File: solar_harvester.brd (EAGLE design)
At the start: 46 x 25.4 mm, 36 parts, among them U1 BQ25505, U2 TPS61322XA, U3 TPS61322XA, U4 MAX17040, U5 INA226, U6 DMP3085LSD

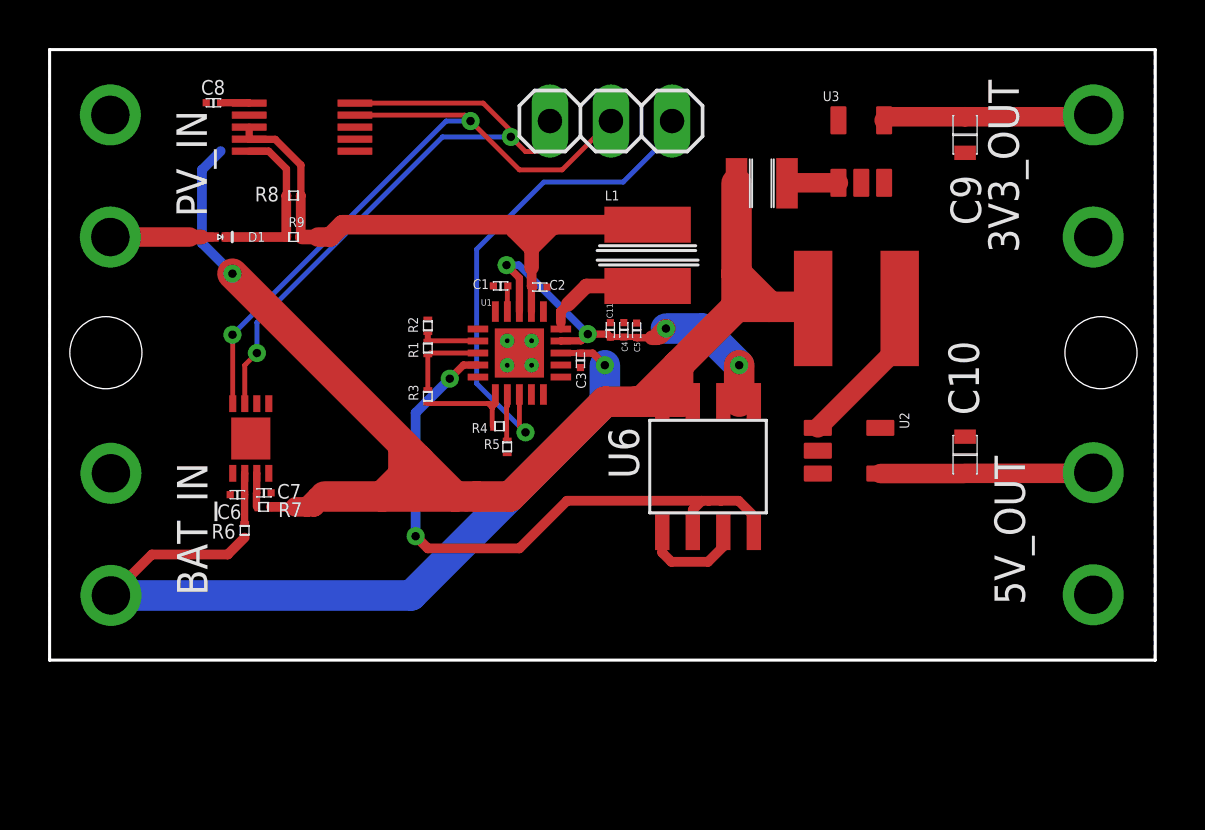
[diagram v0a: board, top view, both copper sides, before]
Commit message: checked pad sizes, embellished board
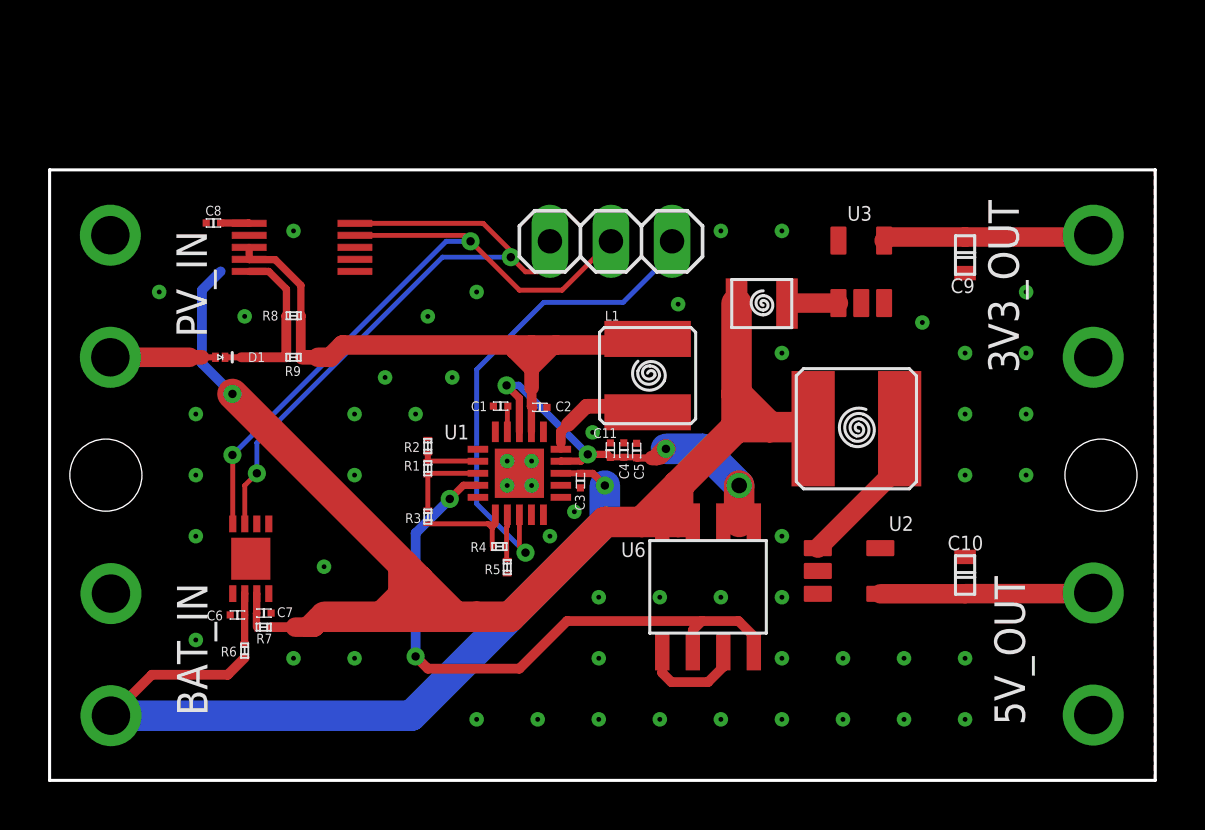
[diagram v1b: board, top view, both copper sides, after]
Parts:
- moved 3V3_OUT 5.00 mm to (43.4, 20.1)
- moved B1 5.00 mm to (23.0, 12.7)
- moved C1 5.00 mm to (18.8, 15.6)
- moved D1 5.00 mm to (7.11, 17.6)
- moved L1 5.00 mm to (24.9, 16.8)
- moved L3 5.00 mm to (29.6, 19.8)
- moved PV_IN 5.00 mm to (2.54, 20.1)
- moved R8 5.00 mm to (10.2, 19.3)
- moved R9 5.00 mm to (10.2, 17.6)
- moved U1 5.00 mm to (19.6, 12.8)
- moved U5 5.00 mm to (10.5, 22.2)
- moved R7 5.00 mm to (8.92, 6.38)
- moved 5V_OUT 5.00 mm to (43.4, 5.26)
- moved BAT_IN 5.00 mm to (2.57, 5.23)
- moved C10 5.00 mm to (38.1, 8.55)
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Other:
- board text added: "HIGH PERFORMANCE COMPUTING AND ARCHITECTURE"
- board text added: "Solar Harvester v1.0"
- board text added: "UJI"
- board text added: "UNIVERSITAT JAUME I"

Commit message: tps, fids added, todo:rev gnd, pass grc
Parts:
- added FID1, U$36: FIDUCIAL_50, vrlib_prod:FEDUCIAL_50
- added TP1, TP2, TP3, TP4, TP5, TP6: TPTP10SQ, testpad:TP10SQ
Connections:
- net GND: now also TP2.TP
- net PVIN_AN: now also TP1.TP
- net VCC: now also TP4.TP
- net VDD3V3: now also TP5.TP
- net VDD5: now also TP6.TP
- net VIN_BAT: now also TP3.TP
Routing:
- net VDD3V3: track 8.69 -> 17.4 mm
- net VDD5: track 8.60 -> 13.0 mm
- net VCC: track 62.6 -> 63.5 mm
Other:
- board text added: "I2C_CONN"

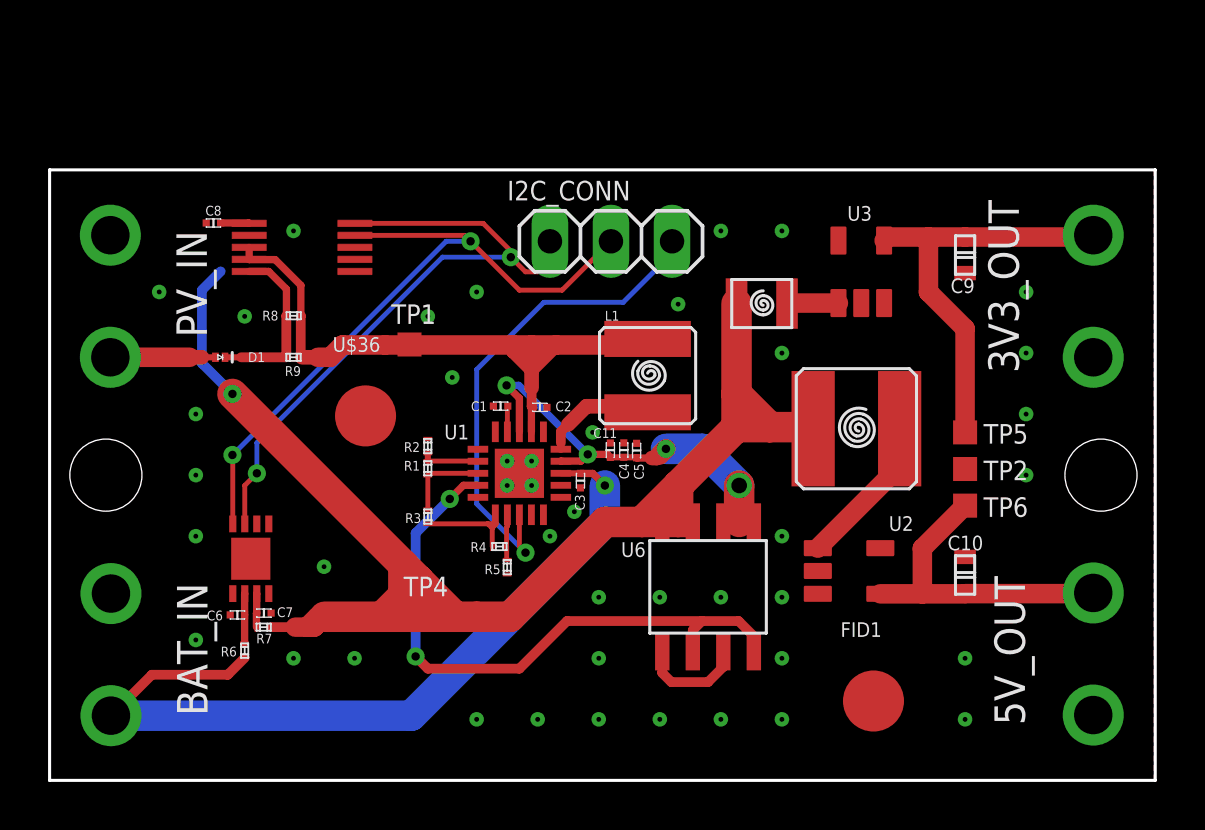
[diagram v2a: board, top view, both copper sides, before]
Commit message: alt measurement ics vin added, drc & gnd rev done
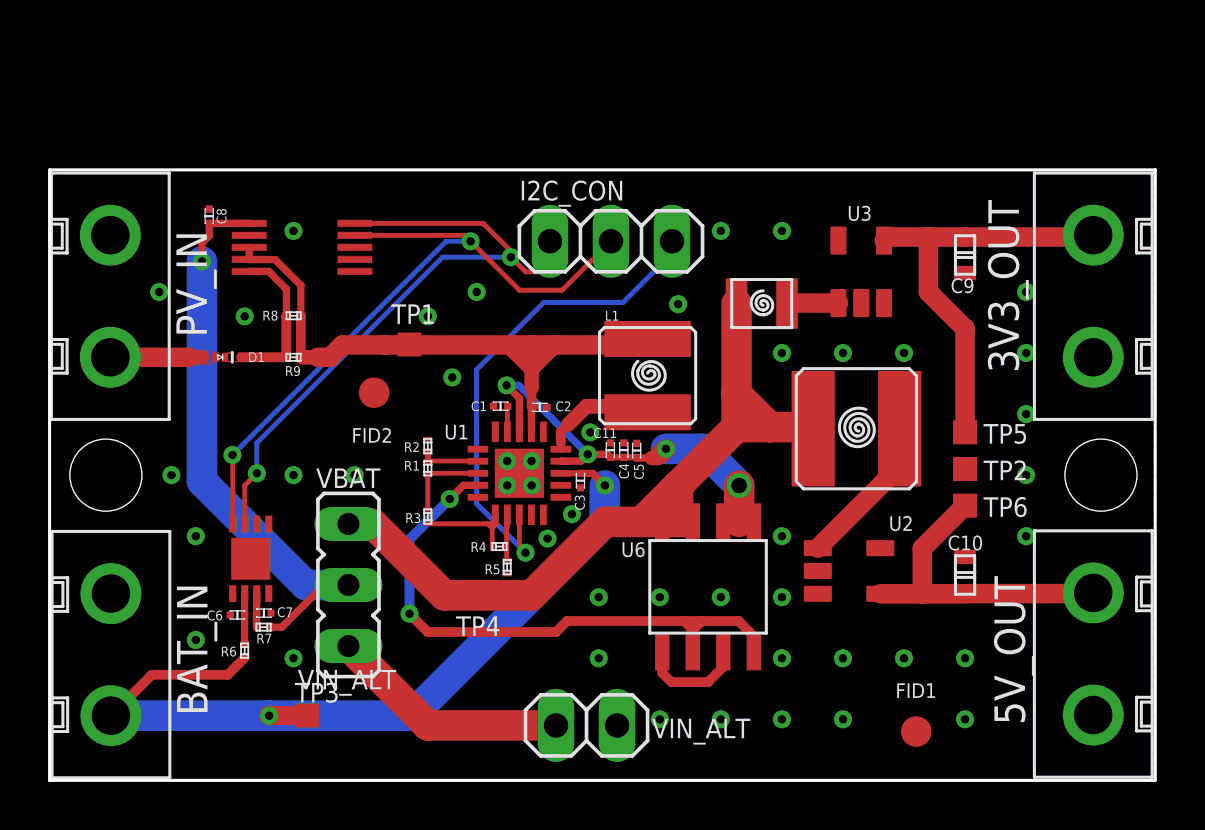
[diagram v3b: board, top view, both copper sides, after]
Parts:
- removed U$36: FIDUCIAL_50, vrlib_prod:FEDUCIAL_50
- added FID2: FIDUCIAL_25, vrlib_prod:FIDUCIAL_25
- added JP3: (no value), pinhead:1X02
- added JP4: (no value), vrlib_jumper:JP2
- B1: value SOLAR_HARVESTER_M1_BOARD -> SOLAR_HARVESTER_V1.0_M1_BOARD; device vrlib_board:SOLAR_HARVESTER_M1_FOOTPRINT -> vrlib_board:SOLAR_HARVESTER_V1.0_M1_FOOTPRINT
- FID1: value FIDUCIAL_50 -> FIDUCIAL_25; device vrlib_prod:FEDUCIAL_50 -> vrlib_prod:FIDUCIAL_25
- moved TP4 2.68 mm to (17.9, 7.70)
- moved FID1 2.18 mm to (36.1, 2.03)
- moved TP3 0.58 mm to (10.7, 2.69), flipped to the top
- moved C8 0.33 mm to (6.65, 23.5), turned to 180 degrees
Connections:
- new net VCC_MIX: C8.1, JP4.2, R7.2, U5.6
- new net VIN_ALT: JP3.2, JP4.3
- net GND: now also JP3.1
- net VCC: now also JP4.1; no longer C8.1, R7.2, U5.6
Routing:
- net VCC: track 63.5 -> 36.3 mm, vias 1 -> 0
- net VCC_MIX: track 0.00 -> 24.4 mm, vias 0 -> 1
- net VIN_ALT: track 0.00 -> 10.0 mm
- net VIN_BAT: track 34.0 -> 35.6 mm, vias 1 -> 2
- net PVIN: track 7.24 -> 6.58 mm
- net N$9: track 4.37 -> 3.81 mm
- net !VB_SEC_ON!: track 26.0 -> 25.5 mm
- added copper zone on layer 1, net N$9
- added copper zone on layer 1, net PVIN
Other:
- board text added: "I2C_CON"
- board text added: "Rev 0"
- board text added: "Solar Harvester v1.0_m1"
- board text added: "VBAT"
- board text added: "VIN_ALT"
- board text removed: "I2C_CONN"
- board text removed: "Solar Harvester v1.0"
